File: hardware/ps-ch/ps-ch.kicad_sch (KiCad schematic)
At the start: 64 parts, among them Q11 MMBT3904, U10 ADuM1401xRW, U11 LMR51610X, U13 ADuM1401xRW, U3 LM61495, U5 OPA992IDCKR

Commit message: calculated voltage correction
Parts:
- removed L5, L6: L, symbol Device:L
- removed R48: R, symbol Device:R
- added C83: 0.1μF 0603 100Vdc X7R ±20%, Capacitor_SMD:C_0603_1608Metric, symbol ps-ch:0.1μF 0603 100Vdc X7R ±20%
- added L5: 33µH, symbol ps-ch:74404064330
- added L6: 60Ω@100MHz, Inductor_SMD:L_0603_1608Metric, symbol ps-ch:74437349015
- added R39: 130kΩ 0603 0.1W ±0.1% ±25ppm/°C, Resistor_SMD:R_0603_1608Metric, symbol ps-ch:130kΩ 0603 0.1W ±0.1% ±25ppm/°C
- added R7: 24kΩ 0603 0.1W ±1% ±100ppm/°C, Resistor_SMD:R_0603_1608Metric, symbol ps-ch:24kΩ 0603 0.1W ±1% ±100ppm/°C
- C25, C49: value C -> 10pF 0603 100Vdc C0G ±5%; footprint (none) -> Capacitor_SMD:C_0603_1608Metric; symbol Device:C -> ps-ch:10pF 0603 100Vdc C0G ±5%; DisplayValue0 (none) -> 10pF ±5%; DisplayValue1 (none) -> 0603 100Vdc; DisplayValue2 (none) -> C0G; Manufacturer (none) -> Murata; Manufacturer Part Number (none) -> GCM1885C2A100JA16
- C53, C81: footprint Capacitor_SMD:C_0603_1608Metric -> Capacitor_SMD:C_0805_2012Metric; symbol ps-ch:0.1μF 0603 100Vdc X7R ±20% -> ps-ch:10μF 0805 50Vdc X5R ±20%; DisplayValue0 0.1μF ±20% -> 10μF ±20%; DisplayValue1 0603 100Vdc -> 0805 50Vdc; DisplayValue2 X7R -> X5R; Manufacturer Part Number GRM188R72A104MA35 -> GRM21BR61H106ME43
- R12: value 130kΩ 0805 0.125W ±0.1% ±25ppm/°C -> 130kΩ 0603 0.1W ±0.1% ±25ppm/°C; footprint Resistor_SMD:R_0805_2012Metric -> Resistor_SMD:R_0603_1608Metric; symbol ps-ch:130kΩ 0805 0.125W ±0.1% ±25ppm/°C -> ps-ch:130kΩ 0603 0.1W ±0.1% ±25ppm/°C; DisplayValue1 0805 0.125W -> 0603 0.1W; Manufacturer Part Number RT0805BRD07130KL -> RT0603BRD07130KL
- R13, R16: value 7.15kΩ 0805 0.125W ±0.1% ±25ppm/°C -> 7.15kΩ 0603 0.1W ±0.1% ±25ppm/°C; footprint Resistor_SMD:R_0805_2012Metric -> Resistor_SMD:R_0603_1608Metric; symbol ps-ch:7.15kΩ 0805 0.125W ±0.1% ±25ppm/°C -> ps-ch:7.15kΩ 0603 0.1W ±0.1% ±25ppm/°C; DisplayValue1 0805 0.125W -> 0603 0.1W; Manufacturer Part Number RT0805BRD077K15L -> RT0603BRD077K15L
- R14, R62: value 10kΩ 0805 0.125W ±0.1% ±25ppm/°C -> 10kΩ 0603 0.1W ±0.1% ±25ppm/°C; footprint Resistor_SMD:R_0805_2012Metric -> Resistor_SMD:R_0603_1608Metric; symbol ps-ch:10kΩ 0805 0.125W ±0.1% ±25ppm/°C -> ps-ch:10kΩ 0603 0.1W ±0.1% ±25ppm/°C; DisplayValue1 0805 0.125W -> 0603 0.1W; Manufacturer Part Number RT0805BRD0710KL -> RT0603BRD0710KL
- R15: value 10kΩ 0805 0.125W ±0.1% ±25ppm/°C -> 130kΩ 0603 0.1W ±0.1% ±25ppm/°C; footprint Resistor_SMD:R_0805_2012Metric -> Resistor_SMD:R_0603_1608Metric; symbol ps-ch:10kΩ 0805 0.125W ±0.1% ±25ppm/°C -> ps-ch:130kΩ 0603 0.1W ±0.1% ±25ppm/°C; DisplayValue0 10kΩ ±0.1% -> 130kΩ ±0.1%; DisplayValue1 0805 0.125W -> 0603 0.1W; Manufacturer Part Number RT0805BRD0710KL -> RT0603BRD07130KL
- R46: value R -> 75kΩ 0603 0.1W ±1% ±100ppm/°C; footprint (none) -> Resistor_SMD:R_0603_1608Metric; symbol Device:R -> ps-ch:75kΩ 0603 0.1W ±1% ±100ppm/°C; DisplayValue0 (none) -> 75kΩ ±1%; DisplayValue1 (none) -> 0603 0.1W; DisplayValue2 (none) -> ±100ppm; Manufacturer (none) -> Yageo; Manufacturer Part Number (none) -> AC0603FR-0775KL
- R47: value R -> 24kΩ 0603 0.1W ±1% ±100ppm/°C; footprint (none) -> Resistor_SMD:R_0603_1608Metric; symbol Device:R -> ps-ch:24kΩ 0603 0.1W ±1% ±100ppm/°C; DisplayValue0 (none) -> 24kΩ ±1%; DisplayValue1 (none) -> 0603 0.1W; DisplayValue2 (none) -> ±100ppm; Manufacturer (none) -> Yageo; Manufacturer Part Number (none) -> AC0603FR-0724KL
- R50: footprint Resistor_SMD:R_0603_1608Metric -> Resistor_SMD:R_0402_1005Metric; symbol ps-ch:10kΩ 0603 0.1W ±1% ±100ppm/°C -> ps-ch:10kΩ 0402 0.063W ±1% ±100ppm/°C; DisplayValue1 0603 0.1W -> 0402 0.063W; Manufacturer Part Number AC0603FR-0710KL -> AC0402FR-0710KL
- R9: value R -> 0Ω 0603 0.1W ±1% ±100ppm/°C; footprint (none) -> Resistor_SMD:R_0603_1608Metric; symbol Device:R -> ps-ch:0Ω 0603 0.1W ±1% ±100ppm/°C; DisplayValue0 (none) -> 0Ω ±1%; DisplayValue1 (none) -> 0603 0.13W; DisplayValue2 (none) -> ±100ppm; Manufacturer (none) -> Yageo; Manufacturer Part Number (none) -> AC0603FR-070RL
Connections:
- net +3V3: now also C49.2, R46.1, L5.1; no longer C49.1, R46.2
- net GND: now also R47.2, C83.1, R7.2; no longer R47.1
- net VDC: now also L6.2
- net Voltage Correction/VFB: now also R39.2; no longer C25.2
- net at C15.2, C16.2, C17.2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: now also C25.2, C83.2; no longer C25.1
- net at C50.2, C51.2, U11.4 (EN)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: now also L6.1
- net at C48.2, U11.6 (SW): now also L5.2
- new net: C49.1, R46.2, R47.1, R7.1, U11.3 (FB)
- new net: C25.1, R39.1
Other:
- note removed: "0R"
- moved on the sheet: C15, C16, C17, C18, C33, C34, C41, C68, L4, R9, U5B

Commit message: wired adc/added resolutions
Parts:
- removed C76: C, symbol Device:C
- added R54: 3kΩ 0603 0.1W ±0.1% ±25ppm/°C, Resistor_SMD:R_0603_1608Metric, symbol ps-ch:3kΩ 0603 0.1W ±0.1% ±25ppm/°C
- added R69: 27kΩ 0603 0.1W ±0.1% ±25ppm/°C, Resistor_SMD:R_0603_1608Metric, symbol ps-ch:27kΩ 0603 0.1W ±0.1% ±25ppm/°C
- added R70, R71: 0Ω 0603 0.1W ±1% ±100ppm/°C, Resistor_SMD:R_0603_1608Metric, symbol ps-ch:0Ω 0603 0.1W ±1% ±100ppm/°C
- R39: value 130kΩ 0603 0.1W ±0.1% ±25ppm/°C -> 4.7kΩ 0603 0.1W ±1% ±100ppm/°C; symbol ps-ch:130kΩ 0603 0.1W ±0.1% ±25ppm/°C -> ps-ch:4.7kΩ 0603 0.1W ±1% ±100ppm/°C; DisplayValue0 130kΩ ±0.1% -> 4.7kΩ ±1%; DisplayValue2 ±25ppm -> ±100ppm; Manufacturer Part Number RT0603BRD07130KL -> AC0603FR-074k7L
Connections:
- net ADC/AIN0 is gone; now on net Current Measurement/IN: C68.1, L9.2, R75.2
- net Current Measurement/OUT: now also R69.2, R71.1
- net GND: now also R54.1
- net at C15.2, C16.2, C17.2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: now also R70.1; no longer C25.2, R12.1, R15.1
- new net: C25.2, R12.1, R15.1, R70.2, R71.2
- new net AIN0: R54.2, R69.1
- no-connect marks 5 -> 4
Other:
- note added: "ferrite!"
- note removed: "scaling, tbd!!!"

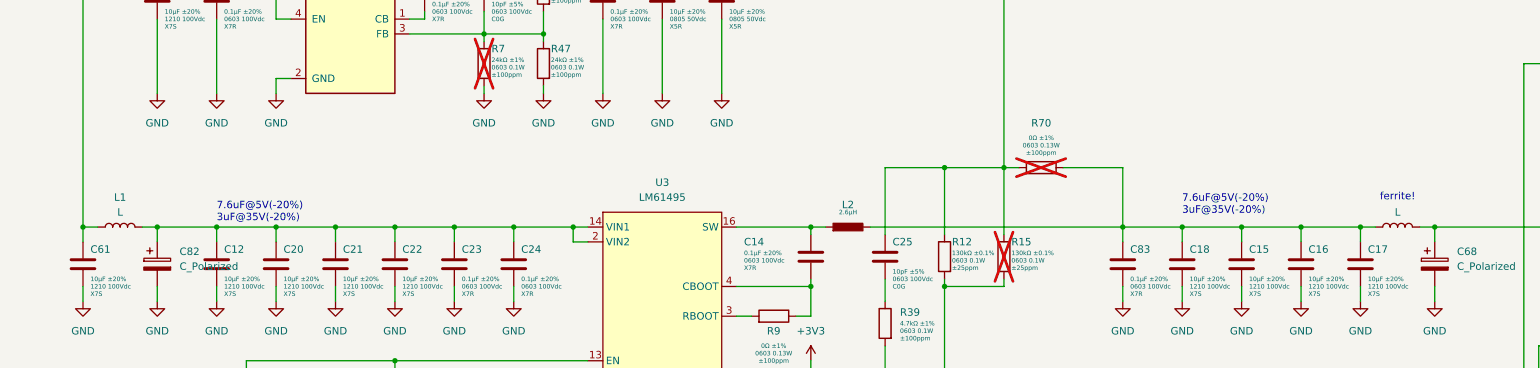
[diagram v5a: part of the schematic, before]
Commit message: parameterized flyback converter
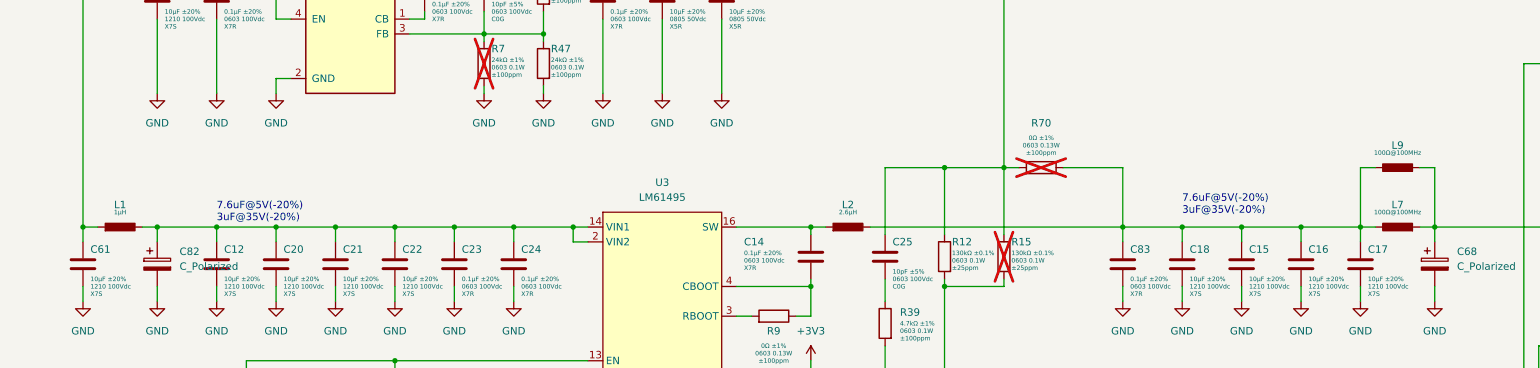
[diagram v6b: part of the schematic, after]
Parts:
- removed L1, L9: L, symbol Device:L
- added L1: 1µH, symbol ps-ch:744316100
- added L7, L9: 100Ω@100MHz, symbol ps-ch:74279224101
- L2: Manufacturer Part Number 74279228600 -> 7443556260
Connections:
- net Current Measurement/IN: now also L7.1, L9.1
- net VDC: now also L1.2
- net at C12.2, C20.2, C21.2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: now also L1.1
- net at C15.2, C16.2, C17.2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: now also L7.2, L9.2
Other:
- note removed: "ferrite!"

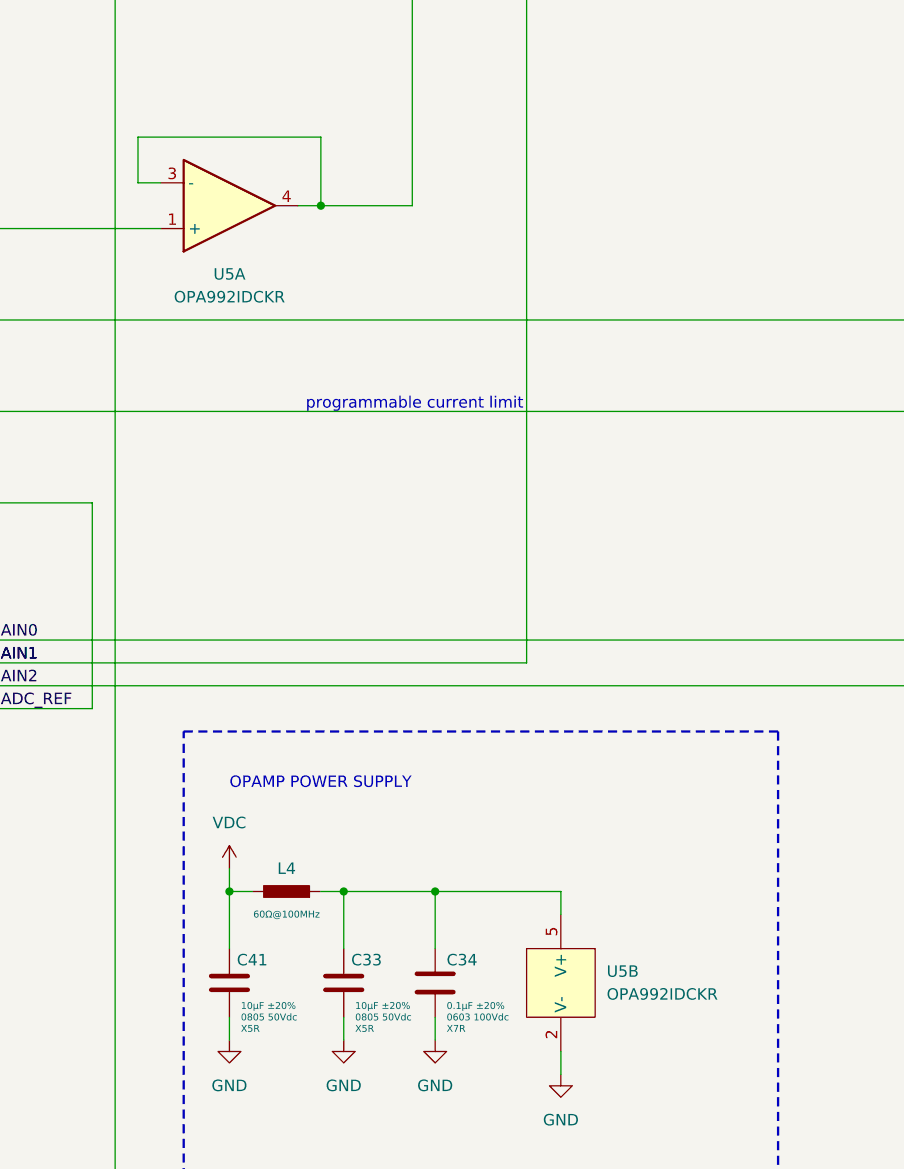
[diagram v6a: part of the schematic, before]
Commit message: changed voltage regulation (preregulator)
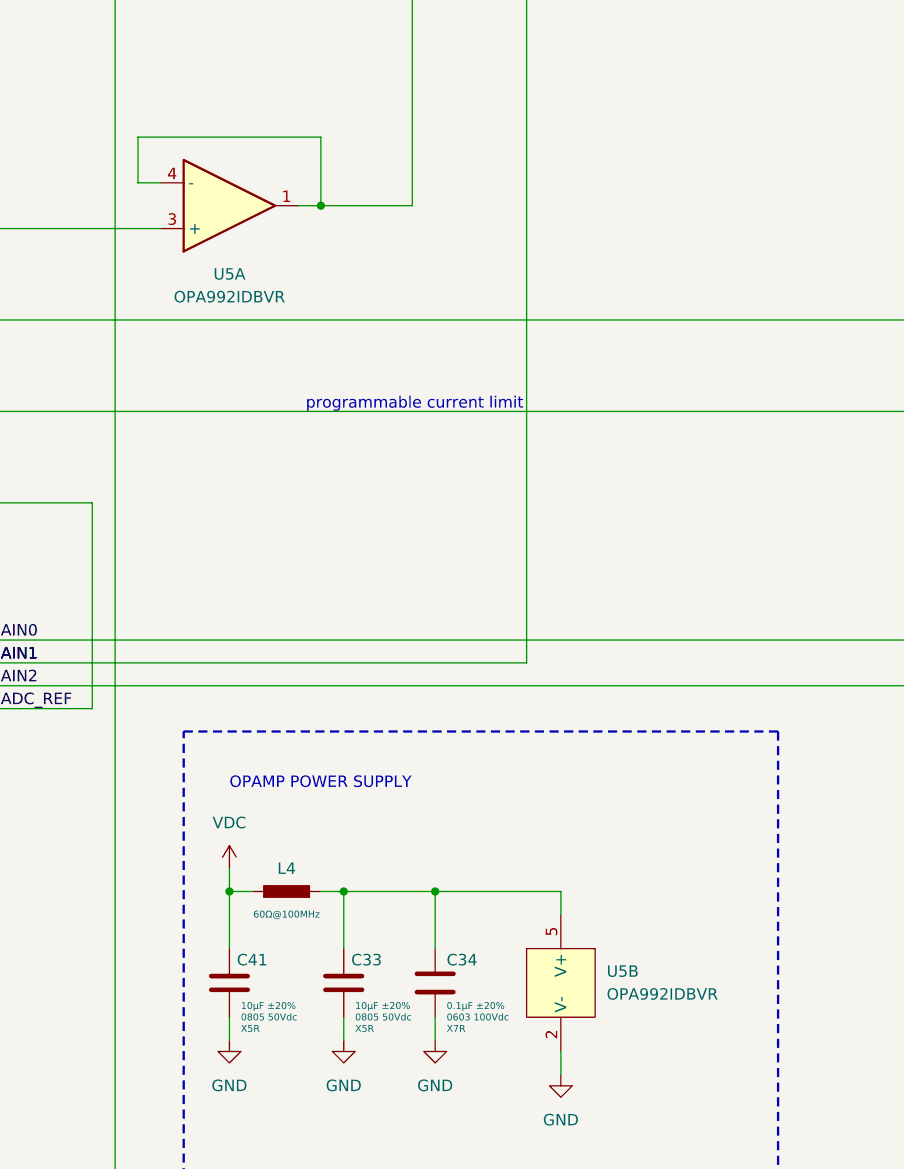
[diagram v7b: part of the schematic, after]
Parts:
- U5: value OPA992IDCKR -> OPA992IDBVR; footprint (none) -> Package_TO_SOT_SMD:SOT-23-5; symbol ps-ch:OPA992IDCKR -> ps-ch:OPA992IDBVR; Manufacturer (none) -> Texas Instruments; Manufacturer Part Number (none) -> OPA992IDBVR
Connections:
- net DAC/VOUTA: now also U5.3 (+); no longer U5.1 (+)
- net at R14.1, R62.2, U5.4 (-): now also U5.1; no longer U5.3 (-)
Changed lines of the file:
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@@
 	)
 	(symbol
-		(lib_id "ps-ch:OPA992IDCKR")
+		(lib_id "ps-ch:OPA992IDBVR")
 		(at 309.88 182.88 0)
 		(mirror x)
@@
 			)
 		)
-		(property "Value" "OPA992IDCKR"
+		(property "Value" "OPA992IDBVR"
 			(at 309.88 193.04 0)
 			(effects
@@
 			)
 		)
-		(property "Footprint" ""
-			(at 309.88 182.88 0)
+		(property "Footprint" "Package_TO_SOT_SMD:SOT-23-5"
+			(at 309.88 193.04 0)
 			(effects
 				(font
@@
 			)
 		)
-		(property "Datasheet" "~"
-			(at 309.88 182.88 0)
+		(property "Datasheet" "https://www.ti.com/lit/ds/symlink/opa2992.pdf?ts=1758720881687&ref_url=https%253A%252F%252Fco.mouser.com%252F"
+			(at 309.88 195.58 0)
 			(effects
 				(font
@@
 			)
 		)
+		(property "Manufacturer" "Texas Instruments"
+			(at 309.88 200.66 0)
+			(effects
+				(font
+					(size 1.27 1.27)
+				)
+				(hide yes)
+			)
+		)
+		(property "Manufacturer Part Number" "OPA992IDBVR"
+			(at 309.88 198.12 0)
+			(effects
+				(font
+					(size 1.27 1.27)
+				)
+				(hide yes)
+			)
+		)
 		(pin "3"
 		)
@@
 	)
 	(symbol
-		(lib_id "ps-ch:OPA992IDCKR")
+		(lib_id "ps-ch:OPA992IDBVR")
 		(at 346.71 269.24 0)
 		(unit 2)
@@
 			)
 		)
-		(property "Value" "OPA992IDCKR"
+		(property "Value" "OPA992IDBVR"
 			(at 351.79 270.5099 0)
 			(effects
@@
 			)
 		)
-		(property "Footprint" ""
-			(at 346.71 269.24 0)
+		(property "Footprint" "Package_TO_SOT_SMD:SOT-23-5"
+			(at 346.71 259.08 0)
 			(effects
 				(font
@@
 			)
 		)
-		(property "Datasheet" "~"
-			(at 346.71 269.24 0)
+		(property "Datasheet" "https://www.ti.com/lit/ds/symlink/opa2992.pdf?ts=1758720881687&ref_url=https%253A%252F%252Fco.mouser.com%252F"
+			(at 346.71 256.54 0)
 			(effects
 				(font
@@
 			(effects
 				(font
+					(size 1.27 1.27)
+				)
+				(hide yes)
+			)
+		)
+		(property "Manufacturer" "Texas Instruments"
+			(at 346.71 251.46 0)
+			(effects
+				(font
+					(size 1.27 1.27)
+				)
+				(hide yes)
+			)
+		)
+		(property "Manufacturer Part Number" "OPA992IDBVR"
+			(at 346.71 254 0)
+			(effects
+				(font
